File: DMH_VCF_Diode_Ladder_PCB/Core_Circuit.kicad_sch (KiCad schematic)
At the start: 52 parts, among them SW1 SW_SPDT, SW2 SW_SPDT, SW3 SW_SPDT, U1 TL074, U2 TL074

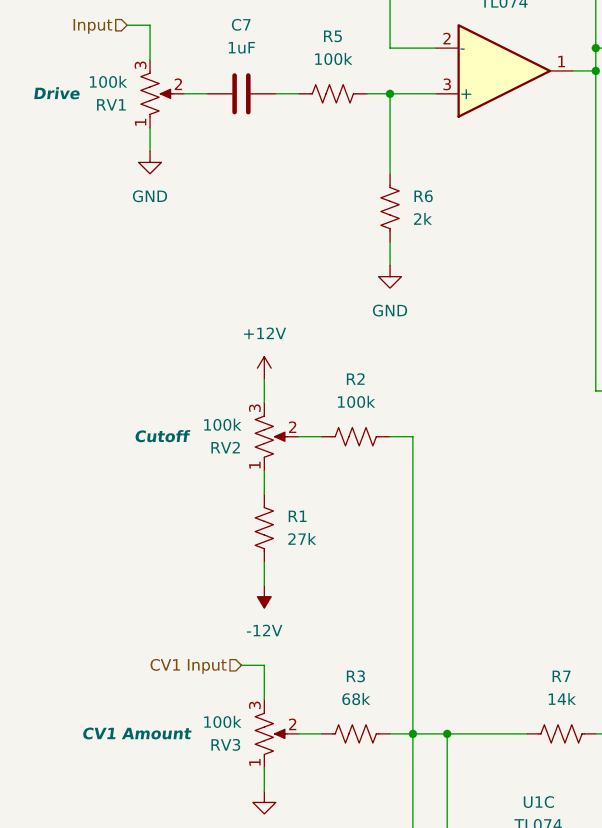
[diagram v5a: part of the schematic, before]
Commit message: Changed cutoff pot limiting resistances in sch
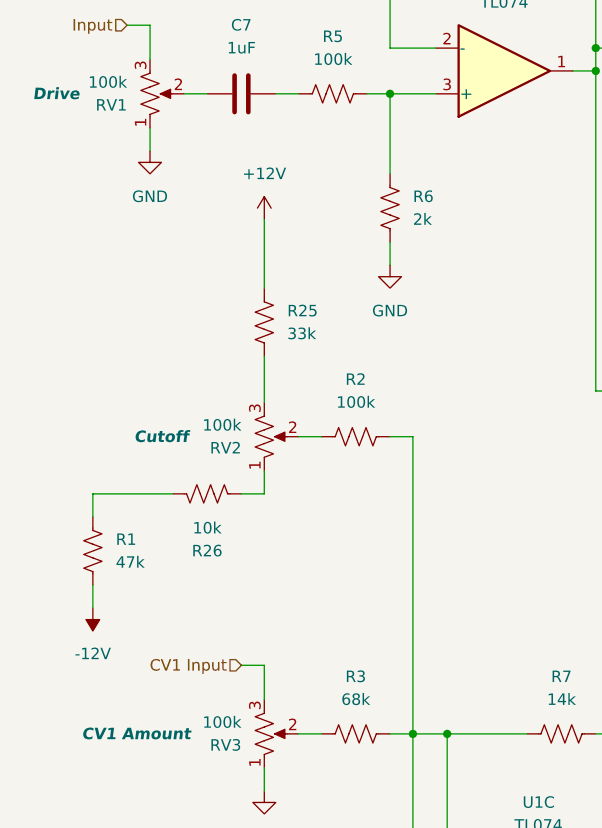
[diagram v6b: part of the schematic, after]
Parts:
- added R25: 33k, Resistor_THT:R_Axial_DIN0207_L6.3mm_D2.5mm_P7.62mm_Horizontal, symbol Device:R_US
- added R26: 10k, Resistor_THT:R_Axial_DIN0207_L6.3mm_D2.5mm_P7.62mm_Horizontal, symbol Device:R_US
- R1: value 27k -> 47k
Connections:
- net +12V: now also R25.1; no longer RV2.3
- net at RV2.1: now also R26.1; no longer R1.1
- new net: R25.2, RV2.3
- new net: R1.1, R26.2
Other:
- moved on the sheet: R1
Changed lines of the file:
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@@
 	(wire
 		(pts
+			(xy 19.05 120.65) (xy 19.05 118.11)
+		)
+		(stroke
+			(width 0)
+			(type default)
+		)
+	)
+	(wire
+		(pts
 			(xy 156.21 111.76) (xy 158.75 111.76)
 		)
@@
 	(wire
 		(pts
+			(xy 35.56 107.95) (xy 38.1 107.95)
+		)
+		(stroke
+			(width 0)
+			(type default)
+		)
+	)
+	(wire
+		(pts
 			(xy 120.65 60.96) (xy 127 60.96)
 		)
@@
 	(wire
 		(pts
-			(xy 38.1 115.57) (xy 38.1 118.11)
+			(xy 146.05 86.36) (xy 146.05 111.76)
 		)
 		(stroke
@@
 	(wire
 		(pts
-			(xy 146.05 86.36) (xy 146.05 111.76)
+			(xy 78.74 152.4) (xy 76.2 152.4)
 		)
 		(stroke
@@
 	(wire
 		(pts
-			(xy 78.74 152.4) (xy 76.2 152.4)
+			(xy 228.6 69.85) (xy 228.6 76.2)
 		)
 		(stroke
@@
 	(wire
 		(pts
-			(xy 228.6 69.85) (xy 228.6 76.2)
+			(xy 19.05 107.95) (xy 27.94 107.95)
 		)
 		(stroke
@@
 	(wire
 		(pts
+			(xy 38.1 107.95) (xy 38.1 105.41)
+		)
+		(stroke
+			(width 0)
+			(type default)
+		)
+	)
+	(wire
+		(pts
 			(xy 203.2 60.96) (xy 198.12 60.96)
 		)
@@
 	(wire
 		(pts
-			(xy 38.1 105.41) (xy 38.1 107.95)
+			(xy 19.05 107.95) (xy 19.05 110.49)
 		)
 		(stroke
@@
 	(wire
 		(pts
-			(xy 38.1 95.25) (xy 38.1 97.79)
+			(xy 38.1 77.47) (xy 38.1 85.09)
 		)
 		(stroke
@@
 	(wire
 		(pts
+			(xy 38.1 92.71) (xy 38.1 97.79)
+		)
+		(stroke
+			(width 0)
+			(type default)
+		)
+	)
+	(wire
+		(pts
 			(xy 212.09 106.68) (xy 212.09 111.76)
 		)
@@
 	)
 	(symbol
+		(lib_id "Device:R_US")
+		(at 38.1 88.9 0)
+		(unit 1)
+		(exclude_from_sim no)
+		(in_bom yes)
+		(on_board yes)
+		(dnp no)
+		(fields_autoplaced yes)
+		(property "Reference" "R25"
+			(at 40.64 87.6299 0)
+			(effects
+				(font
+					(size 1.27 1.27)
+				)
+				(justify left)
+			)
+		)
+		(property "Value" "33k"
+			(at 40.64 90.1699 0)
+			(effects
+				(font
+					(size 1.27 1.27)
+				)
+				(justify left)
+			)
+		)
+		(property "Footprint" "Resistor_THT:R_Axial_DIN0207_L6.3mm_D2.5mm_P7.62mm_Horizontal"
+			(at 39.116 89.154 90)
+			(effects
+				(font
+					(size 1.27 1.27)
+				)
+				(hide yes)
+			)
+		)
+		(property "Datasheet" "~"
+			(at 38.1 88.9 0)
+			(effects
+				(font
+					(size 1.27 1.27)
+				)
+				(hide yes)
+			)
+		)
+		(property "Description" "Resistor, US symbol"
+			(at 38.1 88.9 0)
+			(effects
+				(font
+					(size 1.27 1.27)
+				)
+				(hide yes)
+			)
+		)
+		(pin "2"
+		)
+		(pin "1"
+		)
+		(instances
+			(project "DMH_VCF_Diode_Ladder_PCB"
+				(path "/58f4306d-5387-4983-bb08-41a2313fd315/7ad2d702-dfb7-4d49-a82d-34430dd5948f"
+					(reference "R25")
+					(unit 1)
+				)
+			)
+		)
+	)
+	(symbol
 		(lib_id "power:GND")
 		(at 241.3 118.11 0)
@@
 	(symbol
 		(lib_id "power:+12V")
-		(at 38.1 95.25 0)
+		(at 38.1 77.47 0)
 		(unit 1)
 		(exclude_from_sim no)
@@
 		(fields_autoplaced yes)
 		(property "Reference" "#PWR023"
-			(at 38.1 99.06 0)
+			(at 38.1 81.28 0)
 			(effects
 				(font
@@
 		)
 		(property "Value" "+12V"
-			(at 38.1 90.17 0)
+			(at 38.1 72.39 0)
 			(effects
 				(font
@@
 		)
 		(property "Footprint" ""
-			(at 38.1 95.25 0)
+			(at 38.1 77.47 0)
 			(effects
 				(font
@@
 		)
 		(property "Datasheet" ""
-			(at 38.1 95.25 0)
+			(at 38.1 77.47 0)
 			(effects
 				(font
@@
 		)
 		(property "Description" "Power symbol creates a global label with name \"+12V\""
-			(at 38.1 95.25 0)
+			(at 38.1 77.47 0)
 			(effects
 				(font
@@
 	(symbol
 		(lib_id "Device:R_US")
-		(at 38.1 111.76 0)
+		(at 31.75 107.95 270)
+		(mirror x)
+		(unit 1)
+		(exclude_from_sim no)
+		(in_bom yes)
+		(on_board yes)
+		(dnp no)
+		(property "Reference" "R26"
+			(at 31.75 114.3 90)
+			(effects
+				(font
+					(size 1.27 1.27)
+				)
+			)
+		)
+		(property "Value" "10k"
+			(at 31.75 111.76 90)
+			(effects
+				(font
+					(size 1.27 1.27)
+				)
+			)
+		)
+		(property "Footprint" "Resistor_THT:R_Axial_DIN0207_L6.3mm_D2.5mm_P7.62mm_Horizontal"
+			(at 31.496 106.934 90)
+			(effects
+				(font
+					(size 1.27 1.27)
+				)
+				(hide yes)
+			)
+		)
+		(property "Datasheet" "~"
+			(at 31.75 107.95 0)
+			(effects
+				(font
+					(size 1.27 1.27)
+				)
+				(hide yes)
+			)
+		)
+		(property "Description" "Resistor, US symbol"
+			(at 31.75 107.95 0)
+			(effects
+				(font
+					(size 1.27 1.27)
+				)
+				(hide yes)
+			)
+		)
+		(pin "2"
+		)
+		(pin "1"
+		)
+		(instances
+			(project "DMH_VCF_Diode_Ladder_PCB"
+				(path "/58f4306d-5387-4983-bb08-41a2313fd315/7ad2d702-dfb7-4d49-a82d-34430dd5948f"
+					(reference "R26")
+					(unit 1)
+				)
+			)
+		)
+	)
+	(symbol
+		(lib_id "Device:R_US")
+		(at 19.05 114.3 0)
 		(unit 1)
 		(exclude_from_sim no)
@@
 		(fields_autoplaced yes)
 		(property "Reference" "R1"
-			(at 40.64 110.4899 0)
+			(at 21.59 113.0299 0)
 			(effects
 				(font
@@
 			)
 		)
-		(property "Value" "27k"
-			(at 40.64 113.0299 0)
+		(property "Value" "47k"
+			(at 21.59 115.5699 0)
 			(effects
 				(font
@@
 		)
 		(property "Footprint" "Resistor_THT:R_Axial_DIN0207_L6.3mm_D2.5mm_P7.62mm_Horizontal"
-			(at 39.116 112.014 90)
+			(at 20.066 114.554 90)
 			(effects
 				(font
@@
 		)
 		(property "Datasheet" "~"
-			(at 38.1 111.76 0)
+			(at 19.05 114.3 0)
 			(effects
 				(font
@@
 		)
 		(property "Description" "Resistor, US symbol"
-			(at 38.1 111.76 0)
+			(at 19.05 114.3 0)
 			(effects
 				(font
@@
 	(symbol
 		(lib_id "power:-12V")
-		(at 38.1 118.11 180)
+		(at 19.05 120.65 180)
 		(unit 1)
 		(exclude_from_sim no)
@@
 		(fields_autoplaced yes)
 		(property "Reference" "#PWR022"
-			(at 38.1 114.3 0)
+			(at 19.05 116.84 0)
 			(effects
 				(font
@@
 		)
 		(property "Value" "-12V"
-			(at 38.1 123.19 0)
+			(at 19.05 125.73 0)
 			(effects
 				(font
@@
 		)
 		(property "Footprint" ""
-			(at 38.1 118.11 0)
+			(at 19.05 120.65 0)
 			(effects
 				(font
@@
 		)
 		(property "Datasheet" ""
-			(at 38.1 118.11 0)
+			(at 19.05 120.65 0)
 			(effects
 				(font
@@
 		)
 		(property "Description" "Power symbol creates a global label with name \"-12V\""
-			(at 38.1 118.11 0)
+			(at 19.05 120.65 0)
 			(effects
 				(font
